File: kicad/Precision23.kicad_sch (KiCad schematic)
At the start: 8 parts, among them J501 Conn_01x04_Pin, J502 Conn_01x04_Pin, J503 STANDOFF, J504 STANDOFF, J505 STANDOFF, J506 STANDOFF, U501 SAM-M8Q

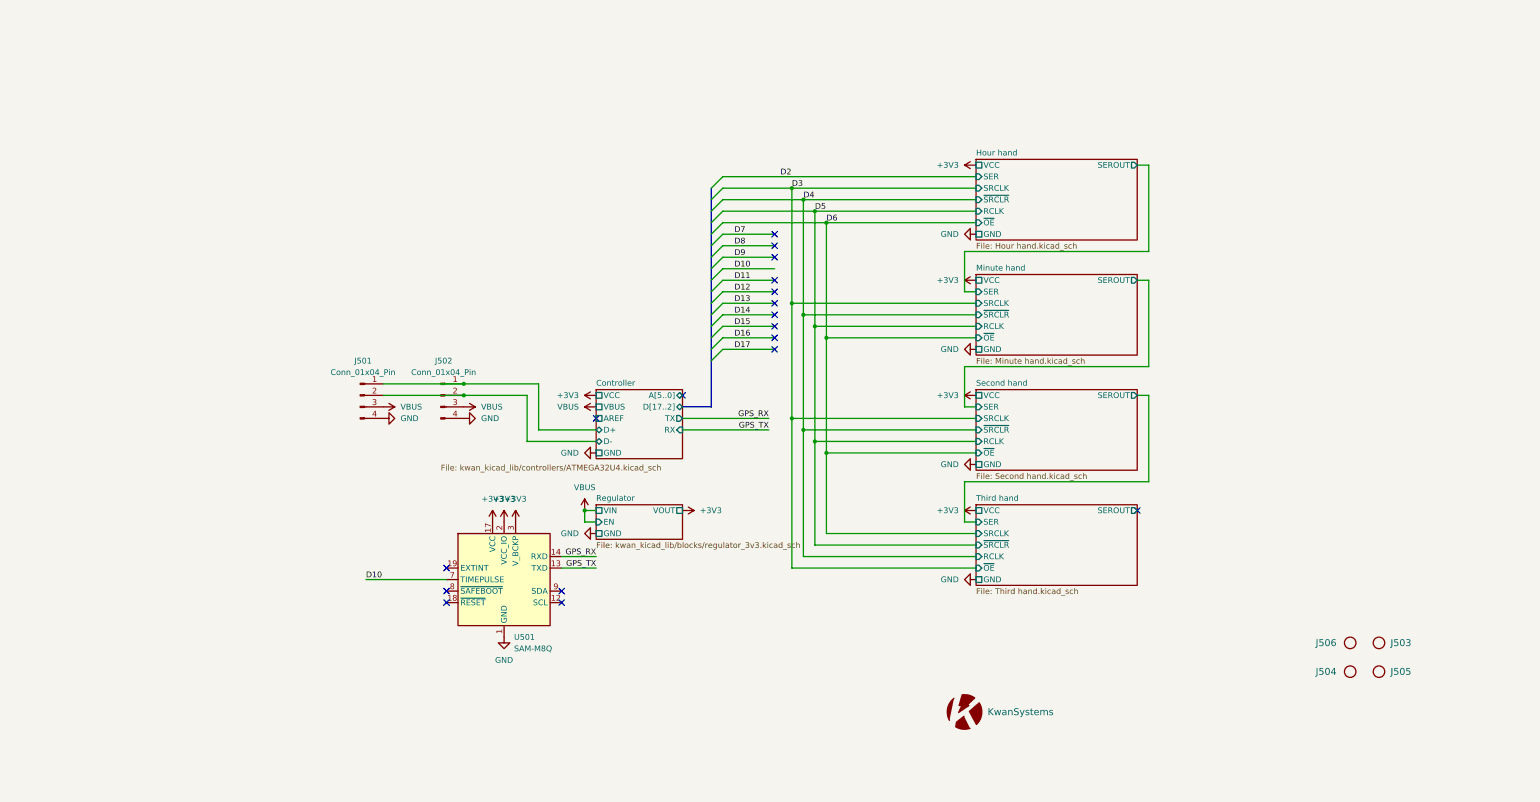
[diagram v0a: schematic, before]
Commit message: Updated to 3 multiplexers
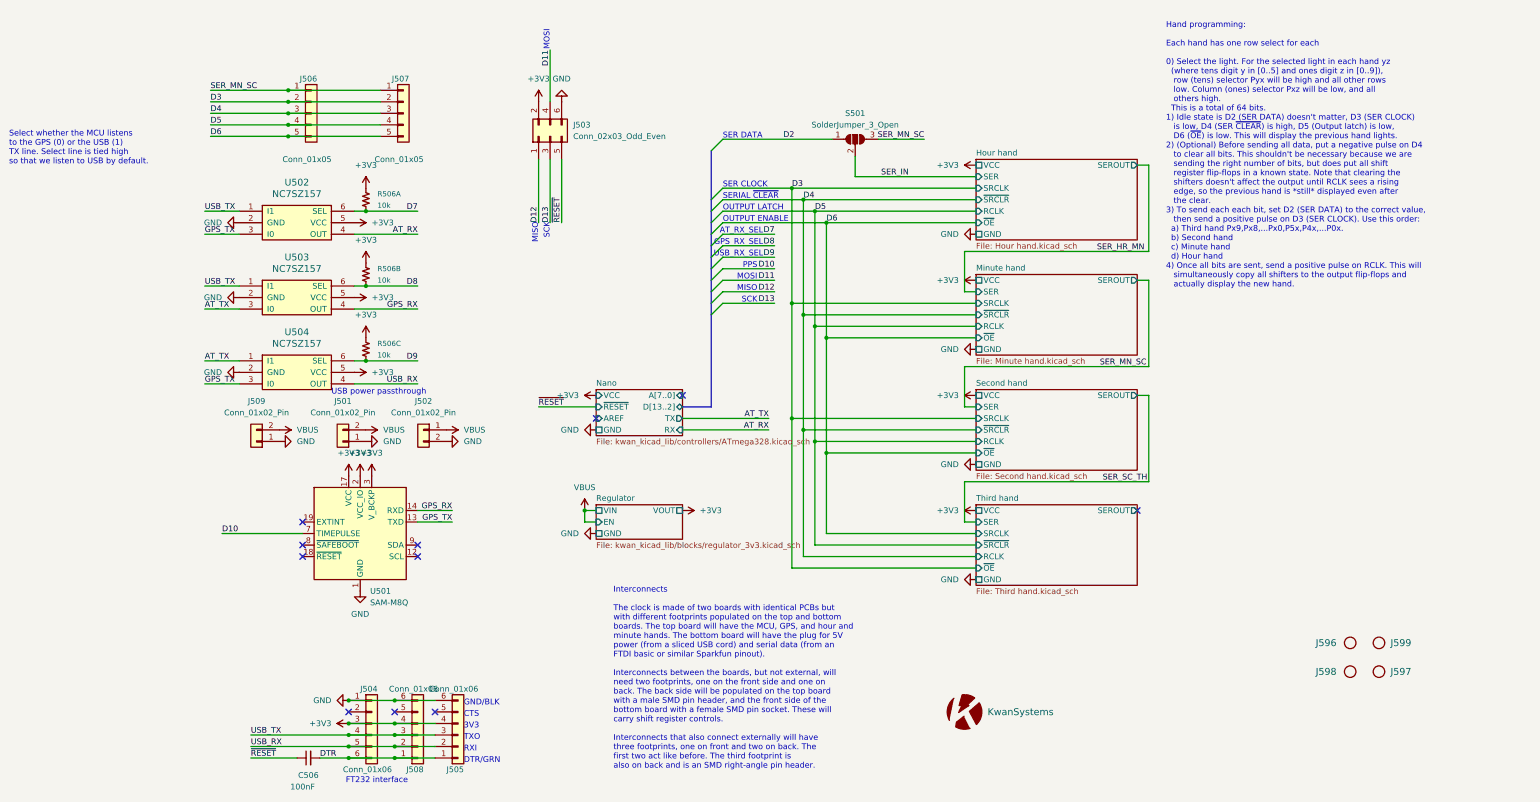
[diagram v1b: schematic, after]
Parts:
- added C506: 100nF, Capacitor_SMD:C_0603_1608Metric, symbol Device:C_Small
- added J503: Conn_02x03_Odd_Even, Connector_PinHeader_2.54mm:PinHeader_2x03_P2.54mm_Vertical_SMD, symbol Connector_Generic:Conn_02x03_Odd_Even
- added J504: Conn_01x06, KwanSystems:SAMTEC_TSM-106-01-T-SH, symbol Connector_Generic:Conn_01x06
- added J505: Conn_01x06, Connector_PinHeader_2.54mm:PinHeader_1x06_P2.54mm_Vertical_SMD_Pin1Left, symbol Connector_Generic:Conn_01x06
- added J506: Conn_01x05, Connector_PinHeader_2.54mm:PinHeader_1x05_P2.54mm_Vertical_SMD_Pin1Left, symbol Connector_Generic:Conn_01x05
- added J507: Conn_01x05, Connector_PinSocket_2.54mm:PinSocket_1x05_P2.54mm_Vertical_SMD_Pin1Left, symbol Connector_Generic:Conn_01x05
- added J508: Conn_01x06, Connector_PinSocket_2.54mm:PinSocket_1x06_P2.54mm_Vertical_SMD_Pin1Left, symbol Connector_Generic:Conn_01x06
- added J509: Conn_01x02_Pin, KwanSystems:SAMTEC_TSM-102-01-T-SH, symbol Connector_Generic:Conn_01x02
- added R506: 10k, KwanSystems:R_Array_Convex_4x0402, symbol KwanSystems:RP4
- added S501: SolderJumper_3_Open, Jumper:SolderJumper-3_P1.3mm_Open_RoundedPad1.0x1.5mm, symbol Jumper:SolderJumper_3_Open
- added U502, U503, U504: NC7SZ157, Package_TO_SOT_SMD:SOT-363_SC-70-6, symbol KwanSystems:NC7SZ157
- J501: value Conn_01x04_Pin -> Conn_01x02_Pin; footprint Connector_PinHeader_2.54mm:PinHeader_1x04_P2.54mm_Vertical_SMD_Pin1Right -> Connector_PinSocket_2.54mm:PinSocket_1x02_P2.54mm_Vertical_SMD_Pin1Left; symbol Connector:Conn_01x04_Pin -> Connector_Generic:Conn_01x02
- J502: value Conn_01x04_Pin -> Conn_01x02_Pin; footprint (none) -> Connector_PinHeader_2.54mm:PinHeader_1x02_P2.54mm_Vertical_SMD_Pin1Left; symbol Connector:Conn_01x04_Pin -> Connector_Generic:Conn_01x02
- renumbered G1 to G101, J506 to J596, J505 to J597, J504 to J598, J503 to J599
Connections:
- net +3V3: now also J503.2 (Pin_2), J504.3 (Pin_3), J505.4 (Pin_4), J508.4 (Pin_4), R506.6 (5), R506.7 (5), R506.8 (5), U502.5 (VCC), U503.5 (VCC), U504.5 (VCC)
- net D11: now also J503.4 (Pin_4)
- net D12: now also J503.1 (Pin_1)
- net D13: now also J503.3 (Pin_3)
- net D2: now also S501.1 (A)
- net D3: now also J506.2 (Pin_2), J507.2 (Pin_2)
- net D4: now also J506.3 (Pin_3), J507.3 (Pin_3)
- net D5: now also J506.4 (Pin_4), J507.4 (Pin_4)
- net D6: now also J506.5 (Pin_5), J507.5 (Pin_5)
- net D7: now also R506.1 (4), U502.6 (SEL)
- net D8: now also R506.2 (4), U503.6 (SEL)
- net D9: now also R506.3 (4), U504.6 (SEL)
- net GND: now also J501.1 (Pin_1), J502.2 (Pin_2), J503.6 (Pin_6), J504.1 (Pin_1), J505.6 (Pin_6), J508.6 (Pin_6), J509.1 (Pin_1), U502.2 (GND), U503.2 (GND), U504.2 (GND); no longer J501.4 (Pin_4), J502.4 (Pin_4)
- net GPS_RX: now also U503.4 (OUT)
- net GPS_TX: now also U502.3 (I0), U504.3 (I0)
- net VBUS: now also J501.2 (Pin_2), J502.1 (Pin_1), J509.2 (Pin_2); no longer J501.3 (Pin_3), J502.3 (Pin_3)
- removed net Controller/D+: J501.1 (Pin_1), J502.1 (Pin_1)
- removed net Controller/D-: J501.2 (Pin_2), J502.2 (Pin_2)
- new net AT_RX: U502.4 (OUT)
- new net AT_TX: U503.3 (I0), U504.1 (I1)
- new net DTR: C506.2, J504.6 (Pin_6), J505.1 (Pin_1), J508.1 (Pin_1)
- new net SER_IN: S501.2 (C)
- new net SER_MN_SC: J506.1 (Pin_1), J507.1 (Pin_1), S501.3 (B)
- new net USB_RX: J504.5 (Pin_5), J505.2 (Pin_2), J508.2 (Pin_2), U504.4 (OUT)
- new net USB_TX: J504.4 (Pin_4), J505.3 (Pin_3), J508.3 (Pin_3), U502.1 (I1), U503.1 (I1)
- new net ~{RESET}: C506.1, J503.5 (Pin_5)
- no-connect marks 18 -> 11
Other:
- removed sheet Controller
- added sheet Nano (kwan_kicad_lib/controllers/ATmega328.kicad_sch)
- note added: "3V3"
- note added: "AT_RX_SEL"
- note added: "CTS"
- note added: "DTR/GRN"
- note added: "FT232 interface"
- note added: "GND/BLK"
- note added: "GPS_RX_SEL"
- note added: "Hand programming: Each hand has one row select for each 0) Select the light. For the selected light in each hand yz (where tens digit y in [0..5] and ones digit z in [0..9]), row (tens) selector Pyx will be high and all other rows low. Column (ones) selector Pxz will be low, and all others high. This is a total of 64 bits. 1) Idle state is D2 (SER DATA) doesn't matter, D3 (SER CLOCK) is low, D4 (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"
- note added: "Interconnects The clock is made of two boards with identical PCBs but with different footprints populated on the top and bottom boards. The top board will have the MCU, GPS, and hour and minute hands. The bottom board will have the plug for 5V power (from a sliced USB cord) and serial data (from an FTDI basic or similar Sparkfun pinout). Interconnects between the boards, but not external, will ne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"
- note added: "MISO"
- note added: "MOSI"
- note added: "OUTPUT ENABLE"
- note added: "OUTPUT LATCH"
- note added: "PPS"
- note added: "RXI"
- note added: "SCK"
- note added: "SER CLOCK"
- note added: "SER DATA"
- note added: "SERIAL ~{CLEAR}"
- note added: "Select whether the MCU listens to the GPS (0) or the USB (1) TX line. Select line is tied high so that we listen to USB by default."
- note added: "TXO"
- note added: "USB power passthrough"
- note added: "USB_RX_SEL"
- moved on the sheet: U501

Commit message: First completely routed version
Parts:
- removed J501: Conn_01x02_Pin, Connector_PinSocket_2.54mm:PinSocket_1x02_P2.54mm_Vertical_SMD_Pin1Left, symbol Connector_Generic:Conn_01x02
- removed J502: Conn_01x02_Pin, Connector_PinHeader_2.54mm:PinHeader_1x02_P2.54mm_Vertical_SMD_Pin1Left, symbol Connector_Generic:Conn_01x02
- removed R506: 10k, KwanSystems:R_Array_Convex_4x0402, symbol KwanSystems:RP4
- removed S501: SolderJumper_3_Open, Jumper:SolderJumper-3_P1.3mm_Open_RoundedPad1.0x1.5mm, symbol Jumper:SolderJumper_3_Open
- added R526, R536, R546: 10k, Resistor_SMD:R_0603_1608Metric, symbol KwanSystems:RESISTOR
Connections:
- net +3V3: now also R526.1, R536.1, R546.1; no longer J504.3 (Pin_3), J508.4 (Pin_4)
- net D3: no longer J507.2 (Pin_2)
- net D4: no longer J507.3 (Pin_3)
- net D5: no longer J507.4 (Pin_4)
- net D6: no longer J507.5 (Pin_5)
- net D7: now also R526.2
- net D8: now also R536.2
- net D9: now also R546.2
- net DTR: no longer J504.6 (Pin_6), J508.1 (Pin_1)
- net GND: no longer J504.1 (Pin_1), J508.6 (Pin_6), J509.1 (Pin_1)
- net SER_MN_SC: no longer J507.1 (Pin_1)
- net USB_RX: no longer J504.5 (Pin_5), J508.2 (Pin_2)
- net USB_TX: no longer J504.4 (Pin_4), J508.3 (Pin_3)
- new net +3.3VP: J504.3 (Pin_3), J508.4 (Pin_4)
- new net D3_BOT: J507.2 (Pin_2)
- new net D4_BOT: J507.3 (Pin_3)
- new net D5_BOT: J507.4 (Pin_4)
- new net D6_BOT: J507.5 (Pin_5)
- new net DTR_BOT: J504.6 (Pin_6), J508.1 (Pin_1)
- new net GNDS: J504.1 (Pin_1), J508.6 (Pin_6), J509.1 (Pin_1)
- new net SER_MN_SC_BOT: J507.1 (Pin_1)
- new net USB_RX_BOT: J504.5 (Pin_5), J508.2 (Pin_2)
- new net USB_TX_BOT: J504.4 (Pin_4), J508.3 (Pin_3)
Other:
- moved on the sheet: C506, J503, J505, J506, J507

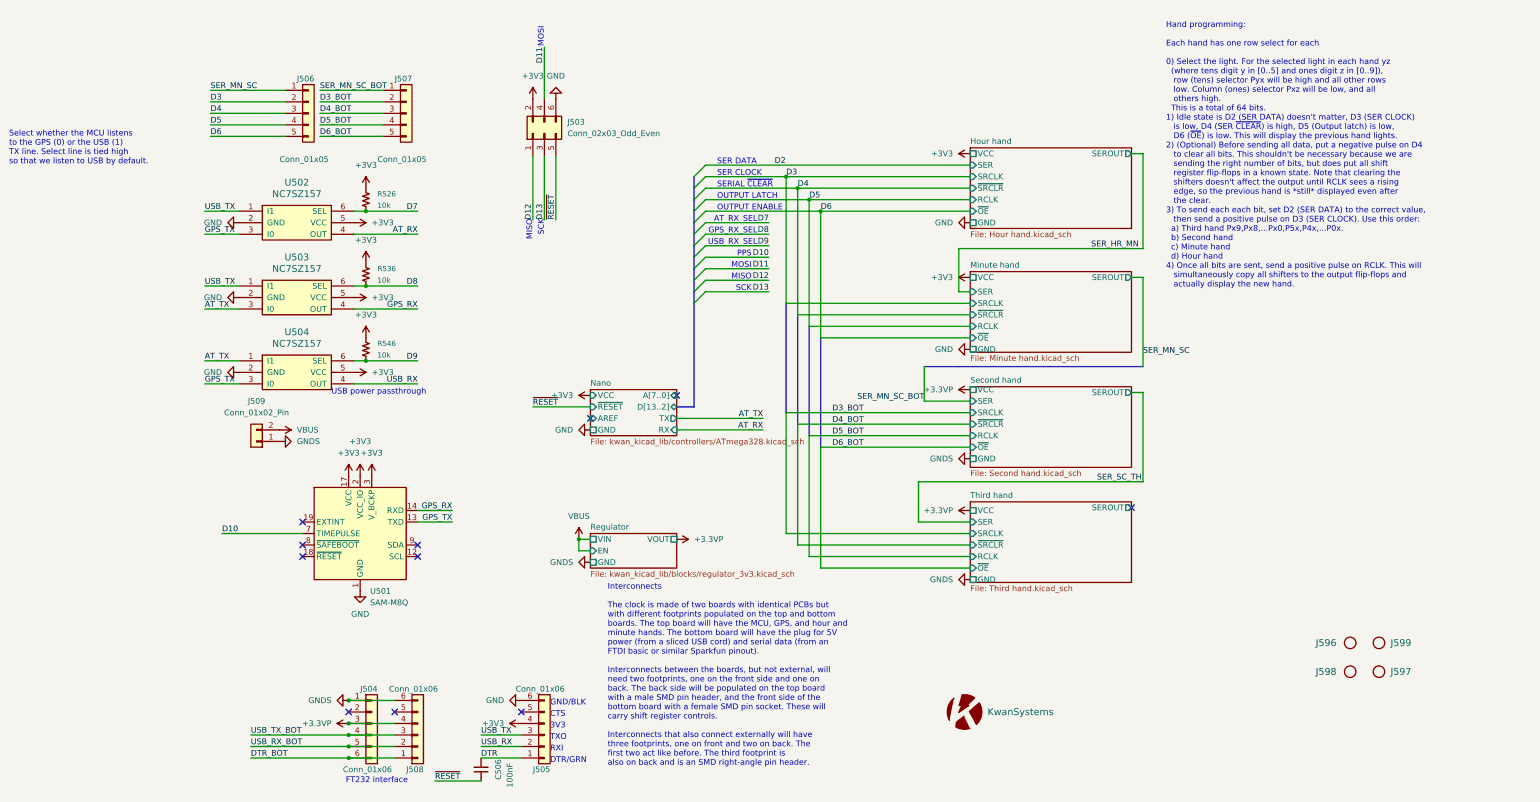
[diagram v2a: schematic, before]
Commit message: Switched PPS to D2 (has external interrupt) and therefore serial data to D10
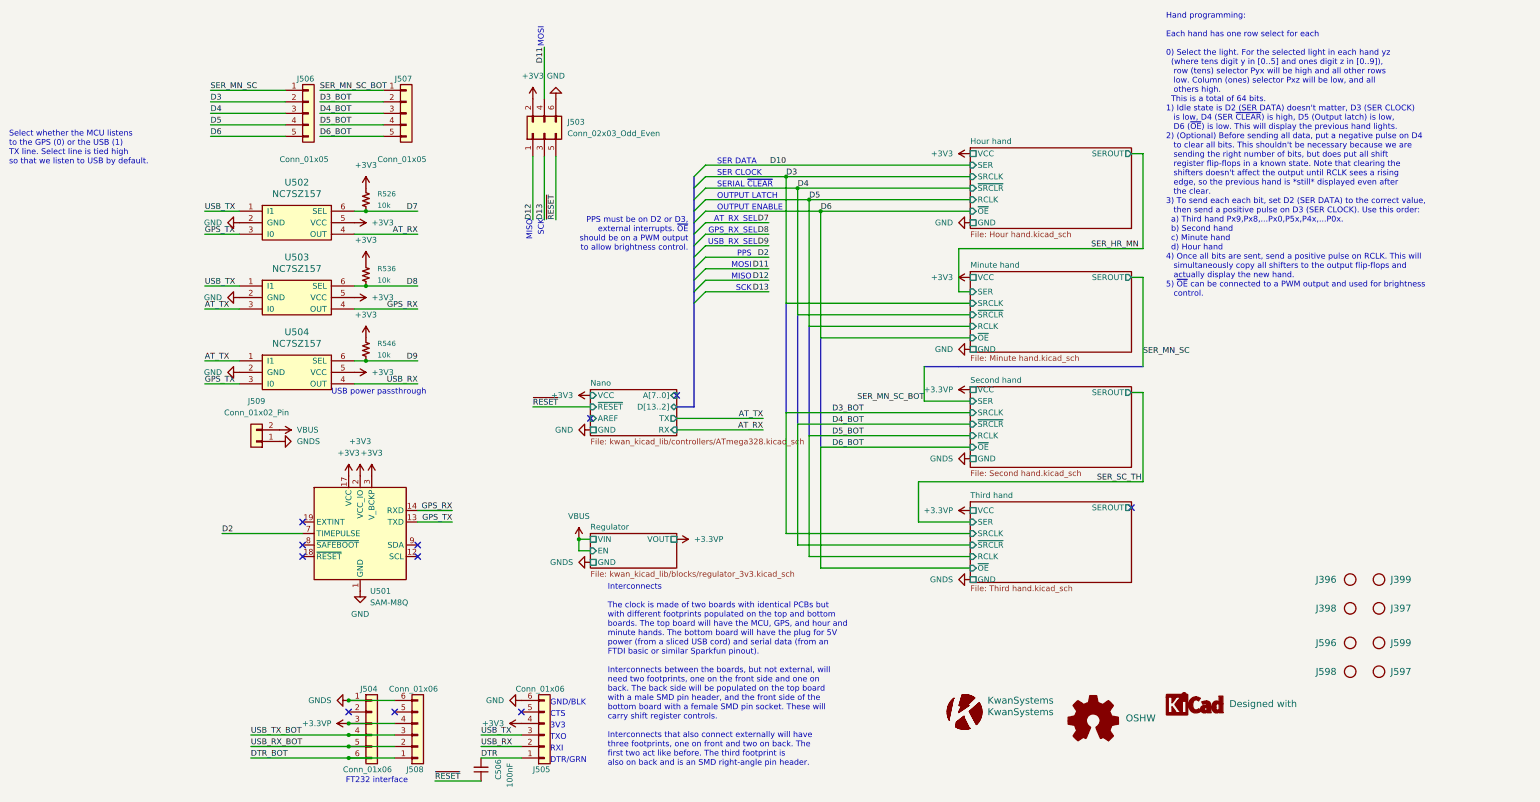
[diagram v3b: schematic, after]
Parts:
- added G102: KwanSystems, KwanSystems:StKwansSoldermask, symbol KwanSystems:KwanSystems
- added G301: OSHW, KwanSystems:OSHW-Symbol_6.7x6mm_SolderMask, symbol KwanSystems:OSHW
- added G302: Designed with, KwanSystems:Symbol_KiCAD-Logo_CopperAndSilkScreenTop_small, symbol KwanSystems:DesignedWithKicad
- added J396, J397, J398, J399: STANDOFF, KwanSystems:STANDOFF_NONPLATED, symbol KwanSystems:STANDOFF
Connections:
- net D10: no longer U501.7 (TIMEPULSE)
- net D2: now also U501.7 (TIMEPULSE)
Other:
- note added: "PPS must be on D2 or D3, external interrupts. ~{OE} should be on a PWM output to allow brightness control."
